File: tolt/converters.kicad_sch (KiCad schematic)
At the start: 51 parts, among them U14 AMS1117-3.3, U15 LP5907MFX-3.3, U16 TPS62173DSG, U19 TLV61047DDC, U24 LTC7138xMSE

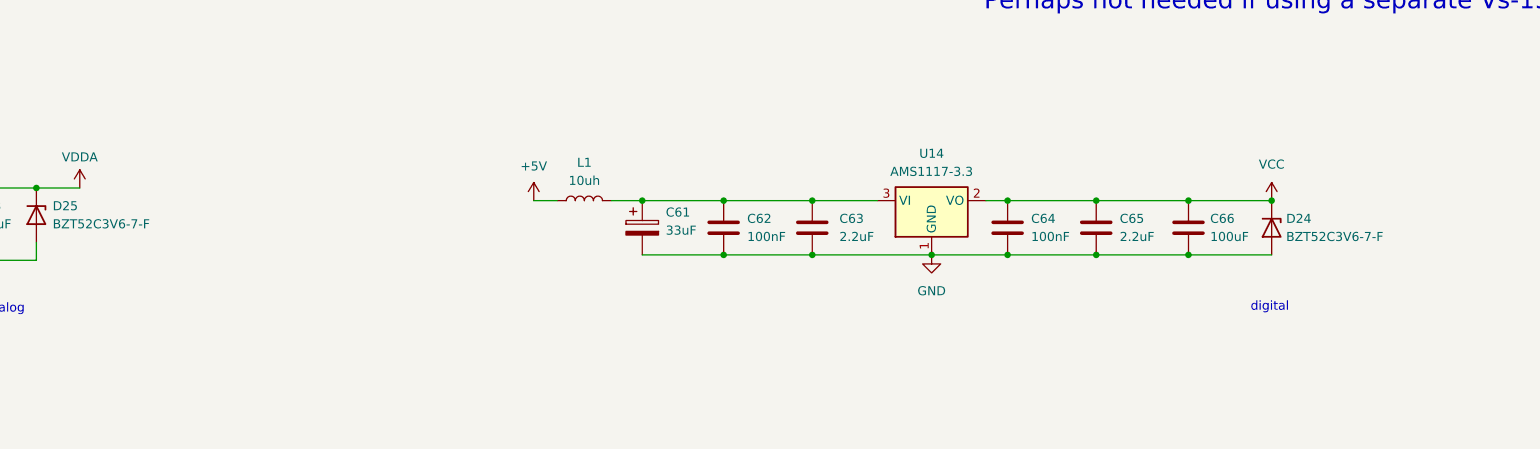
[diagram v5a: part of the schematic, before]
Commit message: some fixed and edit
tbd : phase voltage sensing and adct1 wiring and add on/off switch
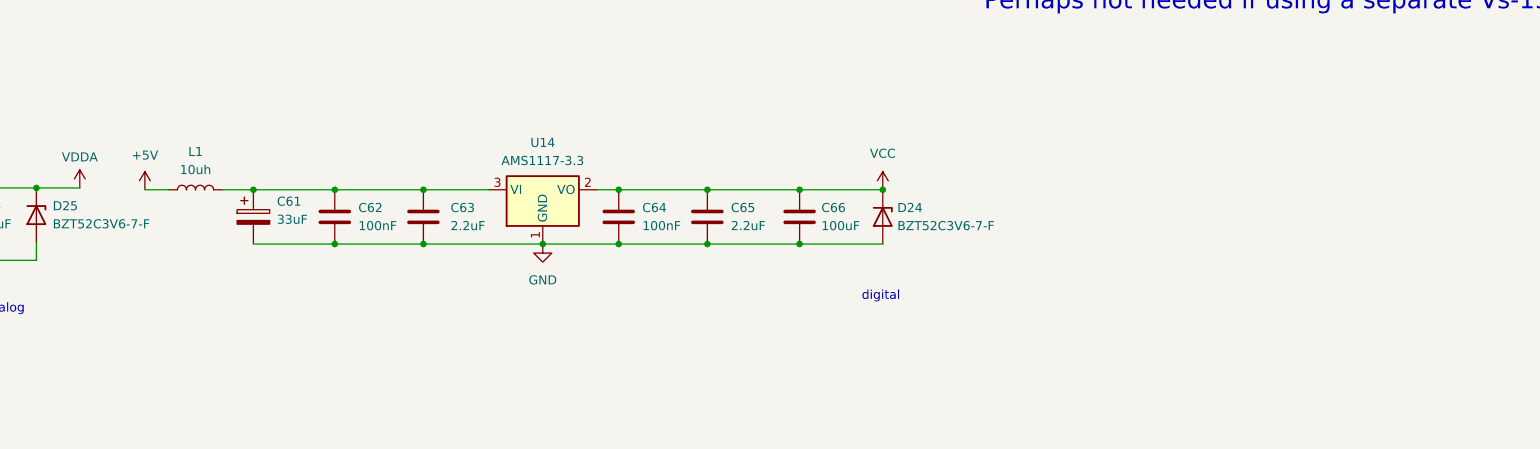
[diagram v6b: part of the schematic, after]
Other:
- moved on the sheet: C61, C62, C63, C64, C65, C66, D24, L1, U14

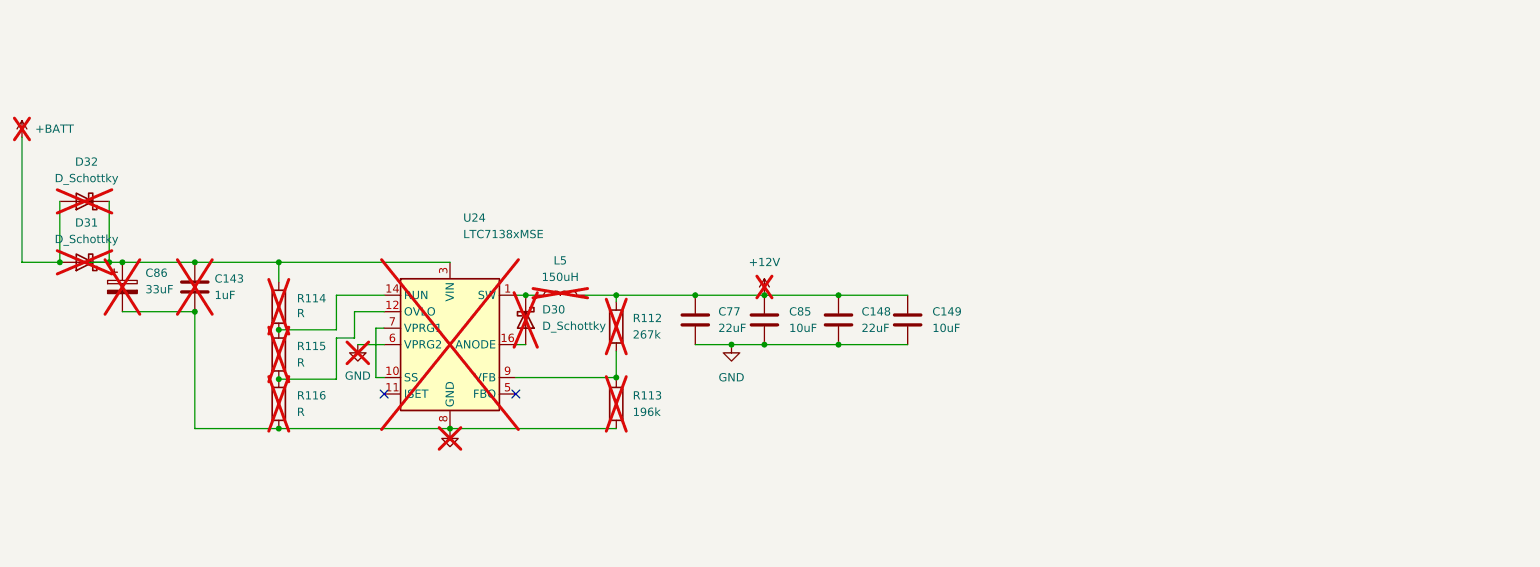
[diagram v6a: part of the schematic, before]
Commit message: added conn for aux 12v
more tbd : add test points
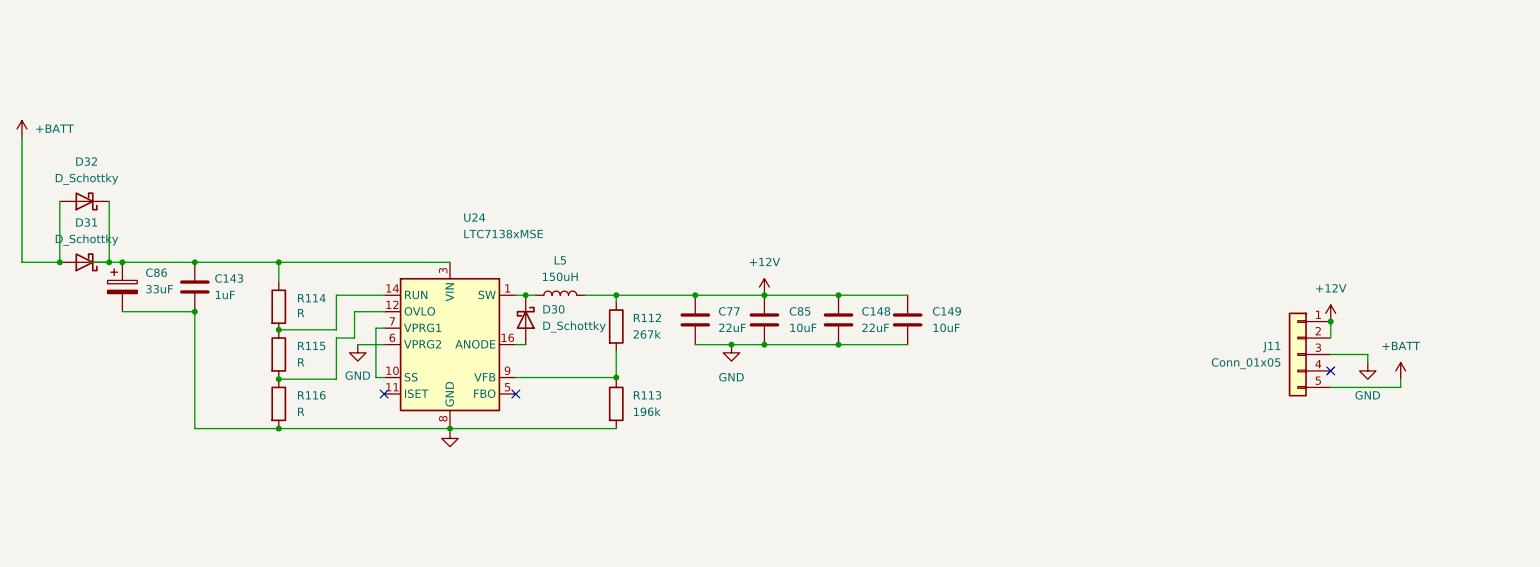
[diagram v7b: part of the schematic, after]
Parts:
- added J11: Conn_01x05, Connector_PinHeader_2.54mm:PinHeader_1x05_P2.54mm_Vertical, symbol Connector_Generic:Conn_01x05
- C143, C86, D30, D31, D32, L5, R112, R113, R114, R115, R116, U24: now fitted
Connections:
- net +12V: now also J11.1 (Pin_1), J11.2 (Pin_2)
- net +BATT: now also J11.5 (Pin_5)
- net GND: now also J11.3 (Pin_3)
- no-connect marks 2 -> 3

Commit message: finished routing
AAAAAAAAAAAAAAAAaaAAAAAAAAAAAAAAAAaaAAAAAAAAAAAAAAAAaaAAAAAAAAAAAAAAAAaaAAAAAAAAAAAAAAAAaaAAAAAAAAAAAAAAAAaaAAAAAAAAAAAAAAAAaaAAAAAAAAAAAAAAAAaaAAAAAAAAAAAAAAAAaaAAAAAAAAAAAAAAAAaaAAAAAAAAAAAAAAAAaa

PLZ WORK PLZ WORK PLZ WORK PLZ WORK PLZ WORK PLZ WORK PLZ WORK PLZ WORK PLZ WORK PLZ WORK PLZ WORK PLZ WORK PLZ WORK PLZ WORK PLZ WORK PLZ WORK PLZ WORK PLZ WORK PLZ WORK PLZ WORK PLZ WORK PLZ WORK PLZ WORK PLZ WORK PLZ WORK PLZ WORK PLZ WORK PLZ WORK PLZ WORK PLZ WORK PLZ WORK PLZ WORK PLZ WORK PLZ WORK PLZ WORK
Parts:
- added C102, C105: 1uf, Capacitor_SMD:C_2220_5750Metric_Pad1.97x5.40mm_HandSolder, symbol Device:C
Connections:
- net +15V is gone; now on net +12V: C75.2, C76.2, D23.1 (K), JP4.1 (A), R95.1
- net +BATT: now also C102.1, C105.1
- net GND: now also C102.2, C105.2
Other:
- note added: "no 12-15v boost"
